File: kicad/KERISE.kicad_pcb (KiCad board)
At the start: 2 copper layers, 40 x 44.5 mm, 119 parts, among them J1 Host, J2 Slave, J3 Host, J4 Slave, J5 COM, J6 Host, J7 Slave, J8 Host, J9 Slave, P1 Motor_L, P10 ENC_Slave, P2 Motor_R, P3 Battery, P4 Fan, P5 ENC_Host, P6 ENC_Slave, P7 ToF_Host, P8 ToF_Slave, P9 ENC_Host, Q1 DMN3065LW-7, Q2 DMN3065LW-7, Q3 DMN3065LW-7, Q4 DMN3065LW-7, Q5 DMN3065LW-7, SW1 SW_Push, SW2 SW_Push, U1 ESP32, U10 TLV316IDCKR, U11 TLV316IDCKR, U12 ICM-20602, U13 PCA9632, U14 LMV321, U2 DRV8835, U3 LXDC2URxx, U4 TLV316IDCKR, U5 TLV316IDCKR, U6 AS5048A, U7 VL53L0X, U8 AS5048A, U9 ICM-20602

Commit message: 自動配線成功
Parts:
- P3: footprint Connectors_Hirose:Hirose_DF13-02P-1.25DSA_02x1.25mm_Straight -> mouse:Hirose_DF13-02P-1.25DSA_02x1.25mm_Straight
- moved C11 3.00 mm to (132.0, 103.5), turned to 0 degrees
- moved C9 3.00 mm to (135.0, 103.5), turned to 180 degrees
- moved C1 1.17 mm to (151.4, 115.0), turned to 0 degrees
- moved C5 0.71 mm to (150.8, 111.5)
- moved U3 0.71 mm to (150.5, 113.5)
- moved C16 0.50 mm to (138.5, 130.5)
- moved C19 0.50 mm to (158.5, 130.5)
- moved P10 0.50 mm to (160.5, 128.5)
- moved P3 0.50 mm to (147.5, 113.0)
- moved P6 0.50 mm to (136.5, 128.5)
- moved U1 0.50 mm to (150.5, 119.5)
- moved U6 0.50 mm to (144.5, 128.5)
- moved U8 0.50 mm to (152.5, 128.5)
- turned R6 to 180 degrees
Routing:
- net /ToF/s_3.3V: track 0.00 -> 17.4 mm, vias 0 -> 2
- net /ToF/s_GND: track 0.00 -> 11.5 mm, vias 0 -> 1
- net /ToF/s_SCL: track 0.00 -> 9.49 mm, vias 0 -> 1
- net /ToF/s_SDA: track 0.00 -> 9.34 mm, vias 0 -> 2
- net +3V3: track 2.06 -> 3.99 mm
- net +BATT: track 25.6 -> 26.3 mm
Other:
- board size 40 x 44.5 mm -> 40 x 66.5 mm
- net class 3.3V: trace_width 0.16 -> 0.18; via_dia 0.5 -> 0.6
- net class Analog: via_dia 0.5 -> 0.6
- net class Antena: clearance 0.18 -> 0.15; trace_width 0.18 -> 0.2; via_dia 0.5 -> 0.6
- net class BATT: via_dia 0.5 -> 0.6
- net class Default: via_dia 0.5 -> 0.6
- net class GND: trace_width 0.16 -> 0.18; via_dia 0.5 -> 0.6
- net class LED: via_dia 0.5 -> 0.6
- net class Motor: via_dia 0.5 -> 0.6
- board text added: "KERISE v5"
- board text removed: "KERISE v3-3"

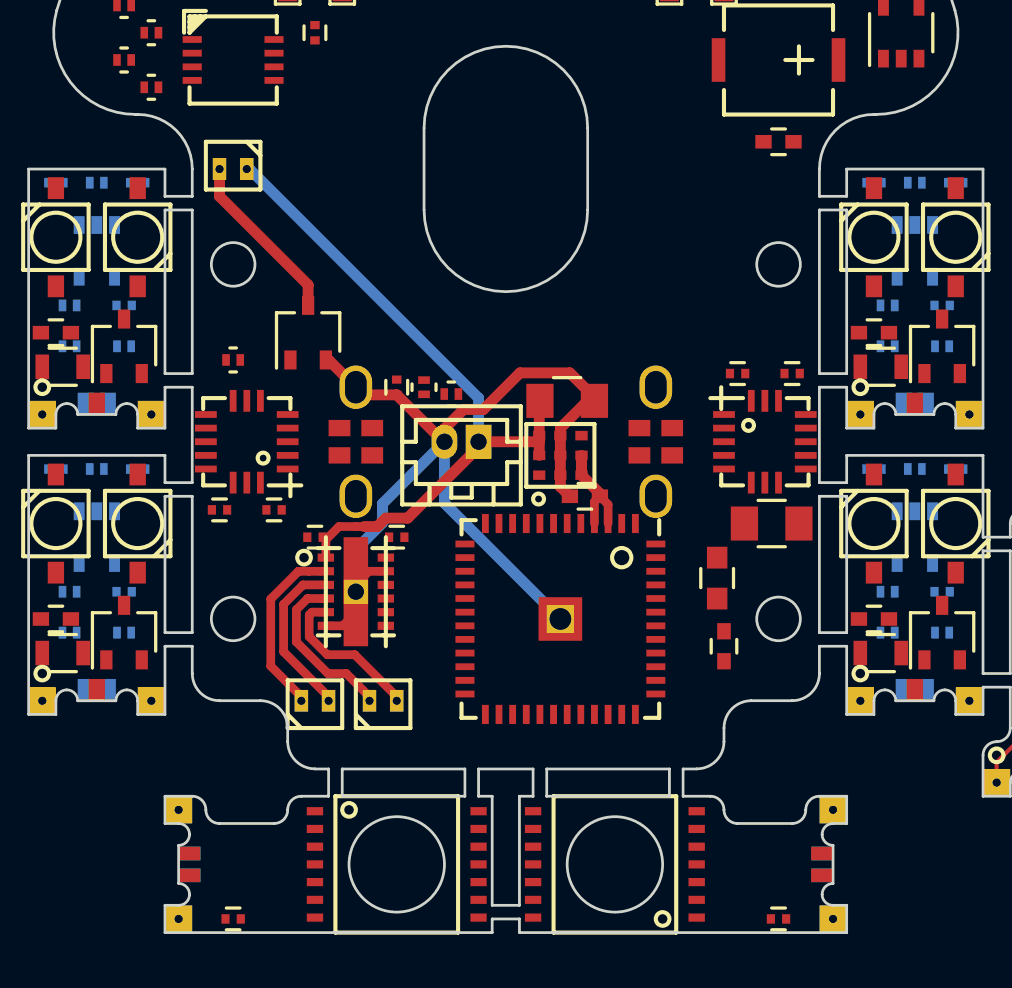
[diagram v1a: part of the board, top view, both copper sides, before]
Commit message: バッテリーコネクタの位置を改良
電池に干渉しないように．
自動配線成功済
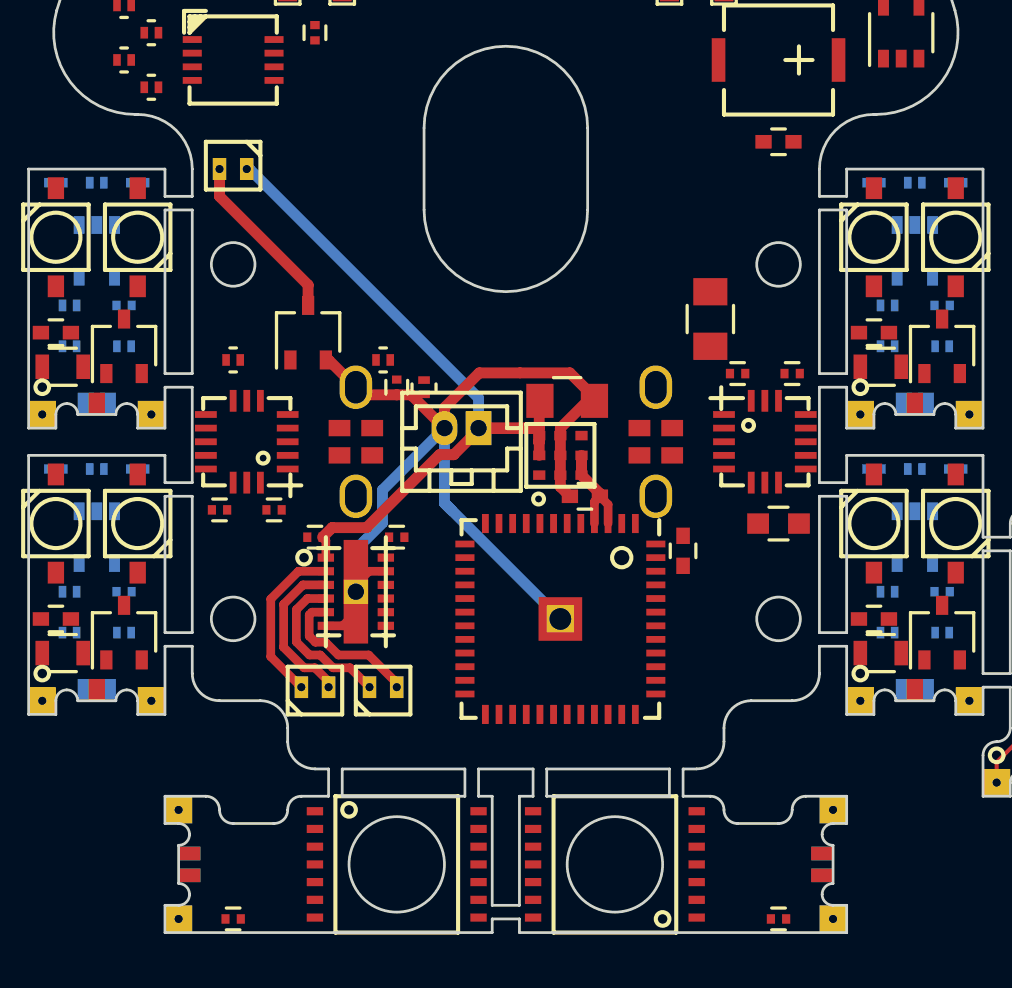
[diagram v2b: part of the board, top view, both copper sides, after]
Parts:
- added G***: LOGO, mouse:KERI_9mm, B.Cu at (148.5, 116.0)
- moved C6 7.83 mm to (156.0, 108.5), turned to 90 degrees
- moved C7 3.81 mm to (155.0, 117.0), turned to 90 degrees
- moved L1 3.01 mm to (158.5, 116.0), turned to 0 degrees
- moved R2 2.80 mm to (144.0, 110.0), turned to 0 degrees
- moved P1 0.50 mm to (141.5, 122.0)
- moved P2 0.50 mm to (144.0, 122.0)
- moved P3 0.50 mm to (147.5, 112.5)
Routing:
- net +BATT: track 26.3 -> 28.2 mm
- net GND: track 36.0 -> 37.1 mm
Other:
- outline, holes or cut-outs redrawn

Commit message: 基板発注
KERISEv5初版はこのデータで発注済
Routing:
- net GND: track 37.1 -> 170.7 mm
- net +3V3: track 3.99 -> 131.6 mm, vias 0 -> 7
- net I2C-SDA: track 0.00 -> 67.9 mm, vias 0 -> 3
- net VDDA: track 0.00 -> 63.8 mm, vias 0 -> 5
- net I2C-SCL: track 0.00 -> 55.5 mm, vias 0 -> 4
- net PR-LED-SR: track 0.00 -> 53.5 mm, vias 0 -> 2
- net BUTTON: track 0.00 -> 46.1 mm, vias 0 -> 2
- net SPI-MISO: track 0.00 -> 41.6 mm, vias 0 -> 2
- net Net-(R1-Pad1): track 0.00 -> 41.3 mm, vias 0 -> 2
- net SPI-SCLK: track 0.00 -> 39.1 mm, vias 0 -> 3
- net PR-LED-SL: track 0.00 -> 37.6 mm, vias 0 -> 2
- net PR-RCV-SL: track 0.00 -> 37.0 mm, vias 0 -> 2
- net SPI-MOSI: track 0.00 -> 37.0 mm, vias 0 -> 4
- net PR-LED-FR: track 0.00 -> 35.4 mm, vias 0 -> 2
- net SPEAKER: track 0.00 -> 34.5 mm, vias 0 -> 2
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
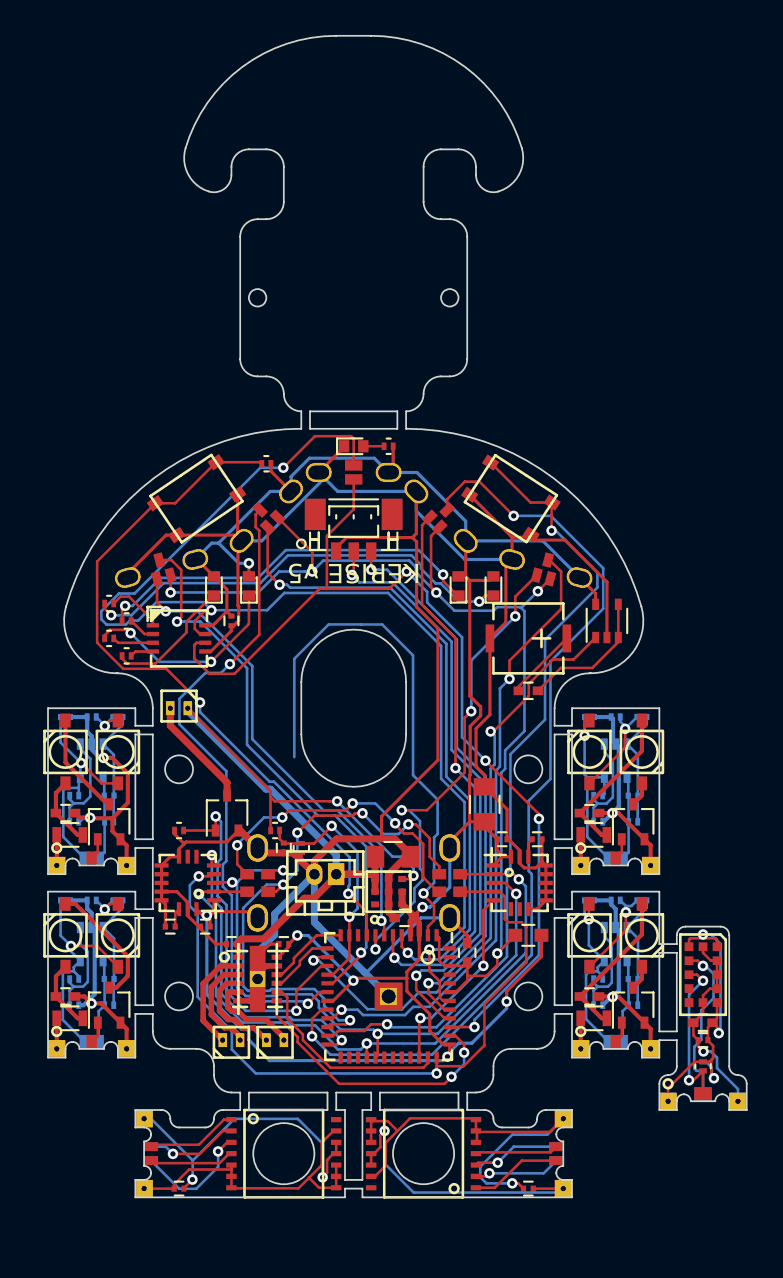
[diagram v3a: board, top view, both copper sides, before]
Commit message: 回路を改良
受光部をフォトトランジスタに変更
測距センサをVL6180Xに変更
動作電圧を3Vに変更
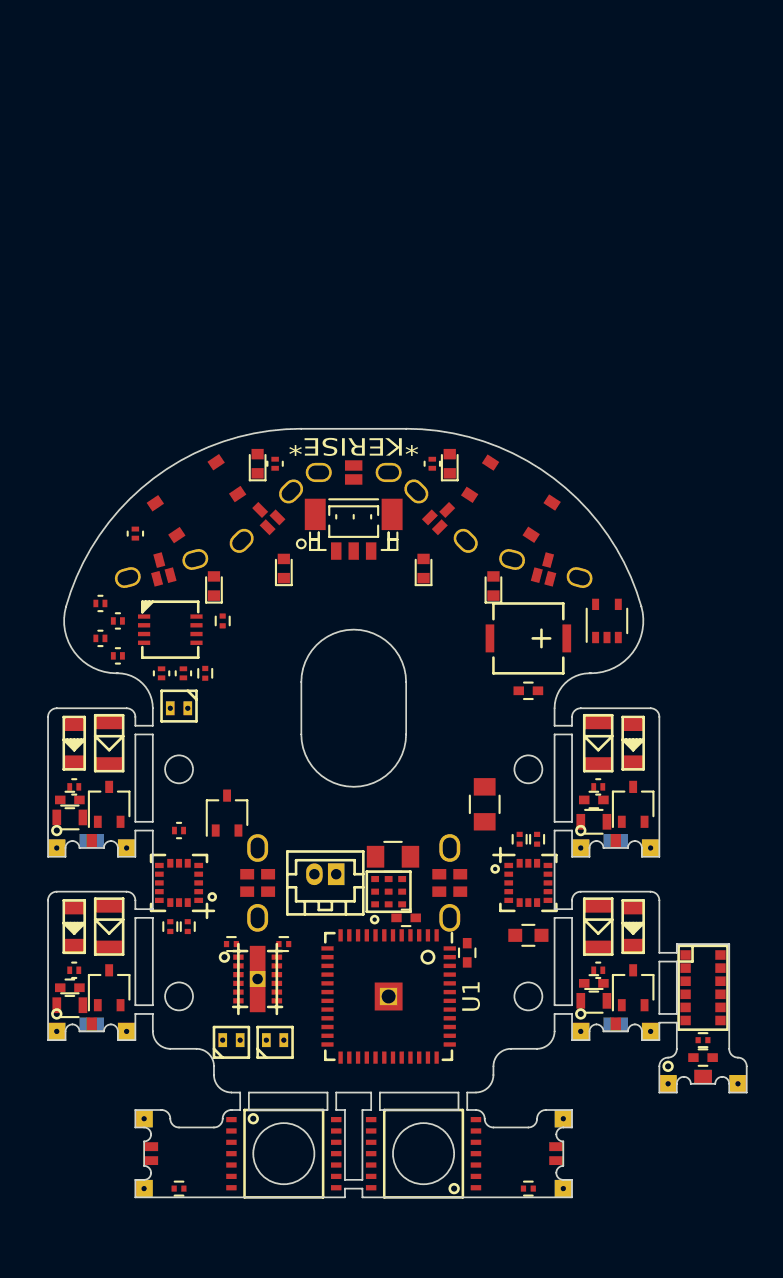
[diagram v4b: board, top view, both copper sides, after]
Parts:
- removed the C10 at (134.5, 108.0)
- removed the C11 at (132.0, 103.5)
- removed the C13 at (135.0, 114.0)
- removed the C14 at (134.5, 118.5)
- removed the C15 at (132.0, 114.0)
- removed C23, C27: 0.01u, Capacitors_SMD:C_0201
- removed C24, C28: 22p, Capacitors_SMD:C_0201
- removed C25, C29: 0.1u, Capacitors_SMD:C_0201
- removed the C9 at (135.0, 103.5)
- removed the D7 at (162.0, 116.0)
- removed the D8 at (165.0, 105.5)
- removed the D9 at (162.0, 105.5)
- removed G***: LOGO, mouse:KERI_9mm
- removed the R12 at (132.5, 118.5)
- removed the R13 at (132.5, 120.0)
- removed the R14 at (134.5, 120.0)
- removed the R16 at (168.5, 123.5)
- removed the R17 at (168.5, 123.5)
- removed R20, R21, R25, R26: 1k, Resistors_SMD:R_0201
- removed R22, R27: 220k, Resistors_SMD:R_0201
- removed the R7 at (132.5, 108.0)
- removed the R8 at (132.5, 109.5)
- removed the R9 at (134.5, 109.5)
- removed the U10 at (163.5, 116.5)
- removed U11: TLV316IDCKR, TO_SOT_Packages_SMD:SOT-353_SC-70-5
- removed U12: ICM-20602, mouse:LGA-16-3x3
- removed the U4 at (133.5, 106.0)
- removed the U9 at (158.0, 113.0)
- added Q2: SFH3015FA, mouse:SFH3015FA, F.Cu at (134.5, 105.0)
- added Q4: SFH3015FA, mouse:SFH3015FA, F.Cu at (134.5, 115.5)
- added Q7: SFH3015FA, mouse:SFH3015FA, F.Cu at (162.5, 115.5)
- added Q9: SFH3015FA, mouse:SFH3015FA, F.Cu at (162.5, 105.0)
- added R5: 1k, Resistors_SMD:R_0201, F.Cu at (153.0, 89.0)
- added U8: ICM-20602, mouse:ICM-20602, F.Cu at (138.5, 113.0)
- C16: renamed from C22; value 1u -> 0.22u
- C17: renamed from C26; value 1u -> 0.22u
- C21: renamed from C33; value 1u -> 10u
- C8: value 1u -> 0.22u
- C9: renamed from C12; value 1u -> 0.22u
- D2: value VSMB294008G -> Power; footprint mouse:VISHAY_DIODE -> LEDs:LED_0402
- D3, D5: value VEMD2020X01 -> SFH4045N; footprint mouse:VISHAY_DIODE -> mouse:SFH4045N
- D4, D6: value VSMB294008G -> SFH4045N; footprint mouse:VISHAY_DIODE -> mouse:SFH4045N
- P10, P6: footprint mouse:STAND_AS_SLAVE -> mouse:STAND_SLAVE_06
- P5, P9: footprint mouse:STAND_AS_HOST -> mouse:STAND_HOST_06
- R12: renamed from R19; value 100k -> 10k; moved to F.Cu
- R14: renamed from R24; value 100k -> 10k; moved to F.Cu
- R2, R3: value 1k -> 10k
- R7: renamed from R6; value 100k -> 10k; moved to F.Cu
- R9: renamed from R11; value 100k -> 10k; moved to F.Cu
- SW1, SW2: footprint mouse:SW_PUSH -> mouse:SKRPACE010
- U1: value ESP32 -> ESP32-PICO-D4
- U3: value LXDC2URxx -> LXDC2UR30
- U5: value TLV316IDCKR -> VL6180X; footprint TO_SOT_Packages_SMD:SOT-353_SC-70-5 -> mouse:VL6180X; moved to F.Cu
- U7: value VL53L0X -> ICM-20602; footprint mouse:VL53L0X -> mouse:ICM-20602
- moved U5 35.1 mm to (168.5, 119.0), turned to 0 degrees
- moved D5 29.5 mm to (164.5, 115.5)
- moved D2 27.5 mm to (154.0, 89.0), turned to 90 degrees
- moved R3 12.1 mm to (138.8, 101.0), turned to 90 degrees
- moved U7 11.3 mm to (158.5, 113.0), turned to 0 degrees
- moved R2 11.1 mm to (137.5, 101.0), turned to 90 degrees
- moved D6 11.0 mm to (164.5, 105.0)
- moved C4 11.0 mm to (140.0, 101.0), turned to 90 degrees
- moved R1 8.50 mm to (136.0, 93.0), turned to 270 degrees
- moved R4 6.58 mm to (144.0, 89.0), turned to 90 degrees
- moved D1 5.59 mm to (143.0, 89.0), turned to 90 degrees
- moved R12 4.12 mm to (162.5, 118.0)
- moved R14 4.12 mm to (162.5, 107.5)
- moved R7 4.12 mm to (132.5, 107.5)
- moved R9 4.12 mm to (132.5, 118.0)
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- renumbered C16 to C10, C17 to C11, C18 to C12, C19 to C13, C20 to C14, C21 to C15, C30 to C18, C31 to C19, C32 to C20, D13 to D10, D10 to D7, D11 to D8, D12 to D9, Q2 to Q3, Q3 to Q5, Q4 to Q6, Q5 to Q8, R15 to R10, R18 to R11, R23 to R13, R28 to R15, R29 to R16, R30 to R17, R31 to R18, R5 to R6, R10 to R8, U14 to U10, U6 to U4, U8 to U6, U13 to U9
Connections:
- C15 pad 1: Net-(C21-Pad1) (its old number) -> Net-(C15-Pad1)
- D2 pad 1: /IR_RCV_SL/LED_to_FET -> GND
- D2 pad 2: /IR_RCV_SL/LED_to_C -> Net-(D2-Pad2)
- D3 pad 1: /IR_RCV_SL/s_AVDD -> /IR_RCV_SL/LED_to_FET
- D3 pad 2: Net-(C9-Pad2) -> /IR_RCV_SL/LED_to_C
- D5 pad 1: /IR_RCV_SR/s_AVDD -> /IR_RCV_FL/LED_to_FET
- D5 pad 2: Net-(C13-Pad2) -> /IR_RCV_FL/LED_to_C
- D6 pad 1: /IR_RCV_FL/LED_to_FET -> /IR_RCV_FR/LED_to_FET
- D6 pad 2: /IR_RCV_FL/LED_to_C -> /IR_RCV_FR/LED_to_C
- R12 pad 1: Net-(C23-Pad2) -> /IR_RCV_FL/s_IR_RCV
- R14 pad 1: Net-(C27-Pad2) -> /IR_RCV_FR/s_IR_RCV
- R7 pad 1: Net-(C9-Pad2) -> /IR_RCV_SL/s_IR_RCV
- R9 pad 1: Net-(C13-Pad2) -> /IR_RCV_SR/s_IR_RCV
- U1 pad 15: FAN -> SPI-CS-AXIS_1
- U1 pad 16: BAT-VOL -> SPI-CS-AXIS_2
- U1 pad 22: SPI-CS-ENC -> SPI-MOSI
- U1 pad 24: SPI-CS-AXIS_1 -> SPI-CS-ENC
- U1 pad 29: SPI-MOSI -> SPI-MISO
- U1 pad 34: SPI-CS-AXIS_2 -> (no net)
- U1 pad 36: SPI-MISO -> FAN
- U5 pad 1: Net-(R12-Pad2) -> (no net)
- U5 pad 2: /IR_RCV_SR/s_GND -> (no net)
- U5 pad 3: Net-(C13-Pad1) -> (no net)
- U5 pad 4: /IR_RCV_SR/s_IR_RCV -> /ToF/s_3.3V
- U5 pad 5: /IR_RCV_SR/s_AVDD -> /ToF/s_SCL
- U7 pad 1: /ToF/s_3.3V -> +3V3
- U7 pad 10: /ToF/s_SCL -> GND
- U7 pad 11: /ToF/s_3.3V -> GND
- U7 pad 12: /ToF/s_GND -> GND
- U7 pad 2: /ToF/s_GND -> SPI-SCLK
- U7 pad 3: /ToF/s_GND -> SPI-MOSI
- U7 pad 4: /ToF/s_GND -> SPI-MISO
- U7 pad 5: /ToF/s_3.3V -> SPI-CS-AXIS_2
- U7 pad 6: /ToF/s_GND -> (no net)
- U7 pad 8: (no net) -> GND
- U7 pad 9: /ToF/s_SDA -> GND
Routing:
- net GND: track 170.7 -> 0.00 mm
- net +3V3: track 131.6 -> 0.00 mm, vias 7 -> 0
- net I2C-SDA: track 67.9 -> 0.00 mm, vias 3 -> 0
- net VDDA: track 63.8 -> 0.00 mm, vias 5 -> 0
- net I2C-SCL: track 55.5 -> 0.00 mm, vias 4 -> 0
- net PR-LED-SR: track 53.5 -> 0.00 mm, vias 2 -> 0
- net +BATT: track 48.3 -> 0.00 mm, vias 2 -> 0
- net BUTTON: track 46.1 -> 0.00 mm, vias 2 -> 0
- net SPI-MISO: track 41.6 -> 0.00 mm, vias 2 -> 0
- net Net-(R1-Pad1): track 41.3 -> 0.00 mm, vias 2 -> 0
- net SPI-SCLK: track 39.1 -> 0.00 mm, vias 3 -> 0
- net PR-LED-SL: track 37.6 -> 0.00 mm, vias 2 -> 0
- net PR-RCV-SL: track 37.0 -> 0.00 mm, vias 2 -> 0
- net SPI-MOSI: track 37.0 -> 0.00 mm, vias 4 -> 0
- net PR-LED-FR: track 35.4 -> 0.00 mm, vias 2 -> 0
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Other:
- board size 40 x 66.5 mm -> 40 x 44 mm
- board text added: "*KERISE*"
- board text removed: "KERISE v5"

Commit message: 電源ラインを配線
あとは自動配線
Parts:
- moved C20 0.50 mm to (141.0, 98.5)
- moved R1 0.50 mm to (136.0, 92.5)
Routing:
- net GND: track 0.00 -> 37.6 mm
- net +BATT: track 0.00 -> 28.0 mm
- net /Motor/MT_OUT_L1: track 0.00 -> 6.14 mm
- net /Motor/MT_OUT_R1: track 0.00 -> 5.89 mm
- net /Motor/MT_OUT_L2: track 0.00 -> 5.80 mm
- net /Motor/MT_OUT_R2: track 0.00 -> 5.51 mm
- net +3V3: track 0.00 -> 4.03 mm

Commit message: 7本残して自動配線終了
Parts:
- moved R15 20.5 mm to (154.5, 96.0), turned to 90 degrees
- moved R16 18.3 mm to (153.0, 94.5), turned to 90 degrees
- moved L1 17.4 mm to (141.5, 119.5), turned to 180 degrees
- moved C7 14.5 mm to (141.0, 120.8), turned to 180 degrees
- moved Q5 12.9 mm to (134.5, 98.0)
- moved P1 12.3 mm to (153.8, 120.5)
- moved P2 12.1 mm to (156.0, 120.5)
- moved U2 12.0 mm to (155.0, 117.5), turned to 0 degrees
- moved C2 11.8 mm to (153.0, 119.0), turned to 270 degrees
- moved R17 11.0 mm to (144.0, 94.5), turned to 90 degrees
- moved R10 10.8 mm to (134.5, 100.0), turned to 0 degrees
- moved C5 10.1 mm to (141.0, 109.0), turned to 270 degrees
- moved U3 9.66 mm to (141.5, 117.0), turned to 90 degrees
- moved C3 9.55 mm to (154.0, 115.5), turned to 270 degrees
- moved R3 9.50 mm to (138.5, 110.5), turned to 180 degrees
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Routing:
- net GND: track 37.6 -> 57.6 mm
- net /ToF/s_3.3V: track 0.00 -> 15.2 mm, vias 0 -> 1
- net /ToF/s_GND: track 0.00 -> 13.0 mm, vias 0 -> 2
- net /Fan/fan_to_fet: track 0.00 -> 7.45 mm
- net +BATT: track 28.0 -> 34.2 mm
- net /ToF/s_SCL: track 0.00 -> 4.61 mm, vias 0 -> 1
- net /Motor/MT_OUT_R1: track 5.89 -> 2.00 mm
- net /ToF/s_SDA: track 0.00 -> 3.88 mm
- net /Motor/MT_OUT_L1: track 6.14 -> 2.32 mm
- net /Motor/MT_OUT_L2: track 5.80 -> 2.11 mm
- net /Motor/MT_OUT_R2: track 5.51 -> 2.21 mm
- net +3V3: track 4.03 -> 5.60 mm
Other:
- outline, holes or cut-outs redrawn
- board text added: "KERISE"
- board text removed: "*KERISE*"
